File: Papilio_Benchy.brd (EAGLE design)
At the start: 101.6 x 55.9 mm, 129 parts, among them IC1 FT2232H, J1 USB MICRO, J4 HDMI-TYPE-A-RECEPTICALFCI1002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, SW1 SWITCH-2CH-6P-3010010P1, SW2 EVQQ2, T1 MOSFET-NCHANNELSMD, U1 ATMEGA32U4-XUMU, U11 PCA9306, U2 LTC3419EMS, U3 93C46B, U5 ARDUINO_MEGA_SHIELD, X2 12MHz, Y1 16MHz KX-7

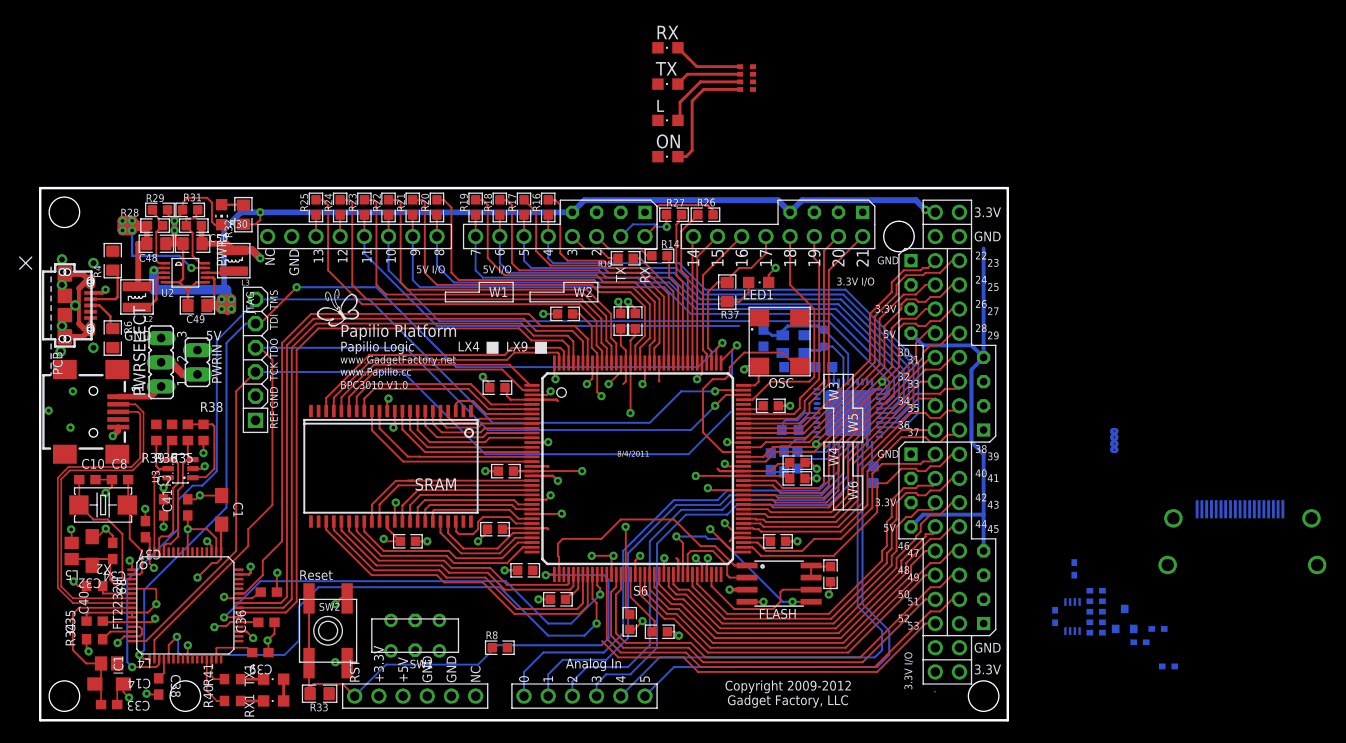
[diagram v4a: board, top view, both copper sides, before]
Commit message: Fully routed except for HDMI and AVR JTAG
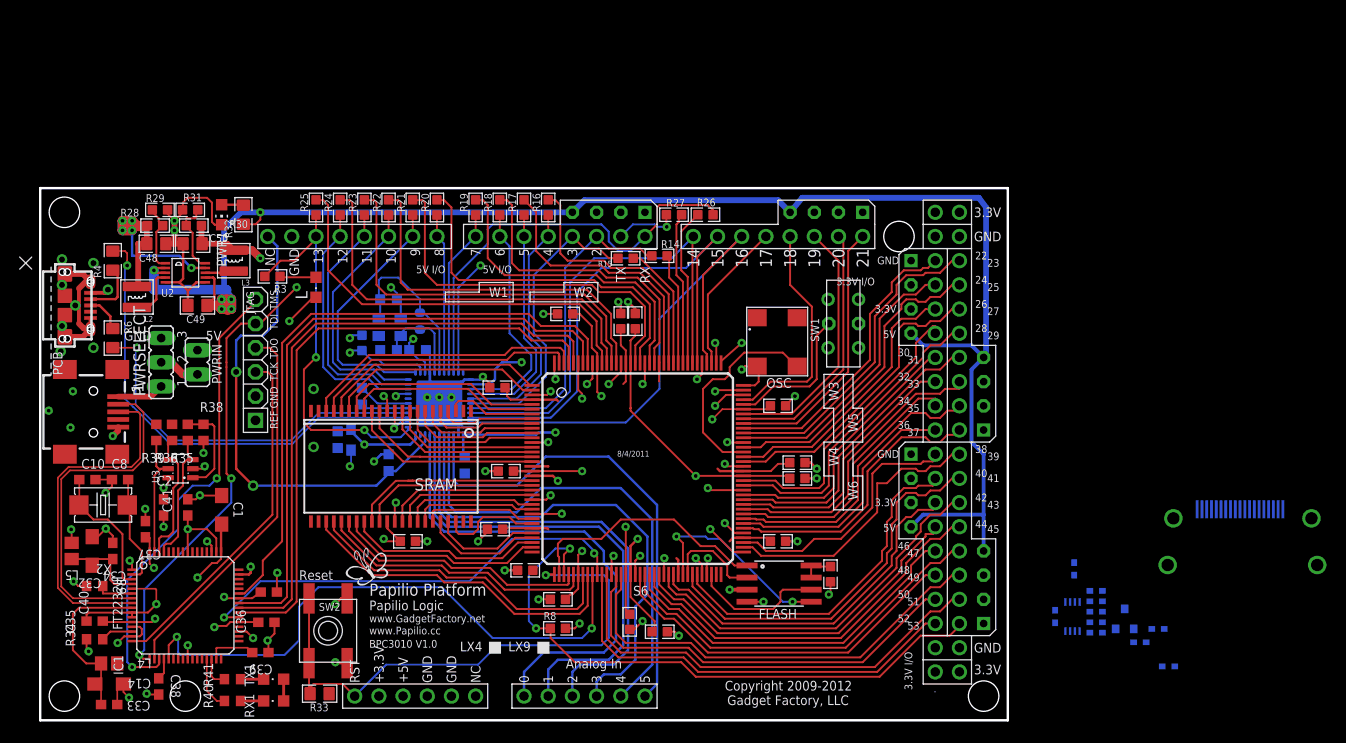
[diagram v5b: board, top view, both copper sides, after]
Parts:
- removed LED1: (no value), led:CHIPLED_0805
- removed ON: Green, led:CHIPLED_0805
- removed R37: 390, GadgetFactory:0805
- removed RN2: 1K, resistor-dil:CAY16
- removed RX, TX: Yellow, led:CHIPLED_0805
- R2: value NM -> 10K; device SmartPrj:R0402 -> GadgetFactory_6.0:0603
- R3: value NM -> 1K; device SmartPrj:R0402 -> GadgetFactory_6.0:0603
- moved R3 90.0 mm to (24.4, 46.6), flipped to the top, turned to 180 degrees
- moved R2 79.7 mm to (33.8, 39.6)
- moved SW1 55.6 mm to (84.3, 41.7), turned to 90 degrees
- moved L6 45.5 mm to (32.6, 29.5), turned to 90 degrees
- moved C5 45.5 mm to (31.2, 29.5), turned to 270 degrees
- moved C7 45.1 mm to (33.8, 34.0), turned to 270 degrees
- moved C4 42.9 mm to (44.6, 26.8)
- moved U1 42.9 mm to (41.9, 33.3)
- moved C6 42.9 mm to (36.6, 27.1)
- moved C3 42.7 mm to (39.6, 38.9), turned to 180 degrees
- moved R1 42.5 mm to (39.9, 41.9)
- moved C9 42.5 mm to (36.6, 38.9)
- moved Y1 42.5 mm to (36.7, 41.3)
- moved L 40.9 mm to (29.0, 45.5), turned to 180 degrees
- moved C11 39.6 mm to (36.6, 44.2), turned to 180 degrees
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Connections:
- net RD+ renamed AVRUSB_P
- net RD- renamed AVRUSB_N
- removed net ATMEGA_D2/SDA: R14.2, U1.19, U5.D2
- removed net ATMEGA_D3/SCL: R15.2, U1.18, U5.D3
- removed net N$3: ON.A, RN2.8
- removed net N$4: RN2.6, TX.A
- removed net N$5: RN2.5, RX.A
- removed net N$7: LED1.A, R37.1
- removed net UGND: C7.2, R3.2, U1.5
- removed net VUSB: U1.7
- new net ATMEGA_D2: R14.2, U1.29, U5.D2
- new net ATMEGA_D3: R15.2, U1.28, U5.D3
- net 3V3: now also C3.1, C4.1, L6.1, R2.2, U1.14, U1.2, U1.34
- net 5V0: no longer C3.1, C4.1, L6.1, RN2.1, RN2.3, RN2.4, U1.13, U1.14, U1.2, U1.34
- net AGND: no longer C6.1, R2.1
- net ARD_RESET: now also R2.1, U1.13
- net AREF: now also U5.AREF
- net ATMEGA_D4: now also U1.27; no longer U1.31
- net ATMEGA_D5*: now also U1.26; no longer U1.30
- net ATMEGA_D6*: now also U1.25; no longer U1.29
- net ATMEGA_D7: now also U1.19; no longer U1.28
- net ATMEGA_IO10*: now also U1.11; no longer U1.25
- net ATMEGA_IO11*: now also U1.10; no longer U1.12
- net ATMEGA_IO12: now also U1.9; no longer U1.1
- net ATMEGA_IO13*: now also R3.2, U1.1; no longer RN2.2, U1.32
- net ATMEGA_IO8: now also U1.18; no longer U1.27
- net ATMEGA_IO9*: now also U1.12; no longer U1.26
- net ATMEGA_RXLED: no longer RX.C
- net ATMEGA_TXLED: no longer TX.C
- net GND: now also C6.1, C7.2, U1.5; no longer LED1.C, ON.C, R2.2, R3.1
- net MEGA_D14: now also U1.30
- net MEGA_D15: now also U1.31
- net MEGA_D16: now also U1.32
- net MEGA_D17: no longer R37.2
- net N$2: now also R3.1; no longer RN2.7
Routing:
- net ARD_RESET: track 0.00 -> 71.5 mm, vias 0 -> 2
- net MEGA_D53: track 0.00 -> 64.0 mm, vias 0 -> 2
- net AVRUSB_N: track 0.00 -> 49.8 mm, vias 0 -> 1
- net 1V2: track 99.3 -> 149.1 mm, vias 6 -> 5
- net ATMEGA_IO8: track 63.9 -> 16.8 mm
- net AREF: track 5.64 -> 51.3 mm, vias 0 -> 2
- net ATMEGA_D7: track 61.6 -> 17.7 mm
- net 3V3: track 137.9 -> 181.6 mm, vias 19 -> 29
- net MEGA_D16: track 15.1 -> 56.0 mm
- net AVRUSB_P: track 0.00 -> 39.9 mm, vias 0 -> 1
- net MEGA_D15: track 14.2 -> 54.1 mm
- net ATMEGA_IO13*: track 2.25 -> 41.8 mm, vias 0 -> 2
- net ATMEGA_IO10*: track 65.8 -> 26.5 mm
- net ATMEGA_IO9*: track 65.5 -> 27.2 mm
- net MEGA_D14: track 13.3 -> 51.1 mm
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- removed copper zone on layer 3, net 1V2
- removed copper zone on layer 3, net AVCC

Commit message: Fully placed and routed! Needs verification and cleanup.
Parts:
- moved J4 44.5 mm to (83.6, 7.74)
- moved R10 44.4 mm to (74.1, 7.38)
- moved R45 43.4 mm to (74.1, 6.08), turned to 180 degrees
- moved R11 42.4 mm to (73.1, 8.45)
- moved R12 40.6 mm to (70.2, 14.4)
- moved R13 40.6 mm to (70.2, 13.3)
- moved R42 40.6 mm to (70.2, 11.1)
- moved R43 40.6 mm to (70.2, 9.96)
- moved R44 40.6 mm to (70.2, 12.2)
- moved T1 40.6 mm to (73.2, 11.4)
- moved U11 40.6 mm to (67.7, 11.7)
- moved C20 40.2 mm to (66.5, 6.97), turned to 180 degrees
- moved R46 38.4 mm to (70.2, 15.6), turned to 180 degrees
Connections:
- removed net ATMEGA_A2: U1.39, U5.A2
- removed net ATMEGA_A3: U1.38, U5.A3
- removed net ATMEGA_A4: U1.37, U5.A4
- removed net ATMEGA_A5: U1.36, U5.A5
- removed net MEGA_D28: S6.88, U5.D28
- removed net MEGA_D30: S6.85, U5.D30
- removed net MEGA_D32: S6.83, U5.D32
- removed net MEGA_D34: S6.81, U5.D34
- new net MEGA_D28/A5: S6.88, U1.36, U5.A5, U5.D28
- new net MEGA_D30/A4: S6.85, U1.37, U5.A4, U5.D30
- new net MEGA_D32/A3: S6.83, U1.38, U5.A3, U5.D32
- new net MEGA_D34/A2: S6.81, U1.39, U5.A2, U5.D34
- net MEGA_D49: now also J4.7; no longer J4.10
- net MEGA_D50: now also J4.9; no longer J4.12
- net MEGA_D51: now also J4.10; no longer J4.7
- net MEGA_D52: now also J4.12; no longer J4.9
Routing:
- net MEGA_D28/A5: track 0.00 -> 98.8 mm, vias 0 -> 1
- net MEGA_D30/A4: track 0.00 -> 95.8 mm, vias 0 -> 1
- net MEGA_D32/A3: track 0.00 -> 94.5 mm, vias 0 -> 1
- net MEGA_D34/A2: track 0.00 -> 92.9 mm, vias 0 -> 1
- net ATMEGA_A3: track 51.5 -> 0.00 mm
- net ATMEGA_A4: track 51.4 -> 0.00 mm
- net ATMEGA_A5: track 50.4 -> 0.00 mm
- net ATMEGA_A2: track 49.5 -> 0.00 mm
- net MEGA_D43: track 40.3 -> 88.0 mm
- net MEGA_D44: track 37.8 -> 80.3 mm
- net DDC_SCL: track 0.00 -> 38.1 mm
- net GND: track 201.8 -> 238.8 mm, vias 74 -> 76
- net MEGA_D28: track 31.3 -> 0.00 mm
- net TX_HDMI_5V: track 0.00 -> 29.3 mm, vias 0 -> 2
- net MEGA_D30: track 28.5 -> 0.00 mm
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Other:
- board text removed: "RN1"
- board text removed: "RN2"
